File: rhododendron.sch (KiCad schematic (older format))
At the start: 43 parts, among them J1 Conn_02x20_Odd_Even, J2 Conn_02x20_Odd_Even, J3 Conn_02x08_Counter_Clockwise, J4 USB-A-SHIELDED, J5 USB-B-SHIELDED, J7 BONUS_ROW, U1 USB3343, Y1 26MHz

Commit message: r0.2: finalize for ordering; improve silkscreen; minor tweaks
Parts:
- added R8: DNP, Resistor_SMD:R_1206_3216Metric, symbol Device:R
- TP10, TP9: footprint TestPoint:TestPoint_Pad_D2.0mm -> gsg-modules:HEADER-1x1
- Y1: symbol Device:Crystal -> Device:Crystal_GND24
- renumbered C9 to C9-DNP1
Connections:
- net GND: now also Y1.2, Y1.4
- net PHY_XO: now also Y1.3; no longer Y1.2
- net TARGET_VBUS: now also R8.1, R8.2
- net PHY_26MHZ_IN renamed PHY_XI
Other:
- note added: "Microchip recommends <1R ESR\non VBUS capacitor. We're recommending DNP\nto limit inrush; the USB spec limits VBUS cap to 10uF."
- note added: "X"
- note removed: "Microchip recommends <1R ESR\non VBUS capacitor."
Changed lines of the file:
@@
 	4500 3650 5200 3650
 $Comp
-L Device:Crystal Y1
+L Device:Crystal_GND24 Y1
 U 1 1 5CD6A676
 P 6050 3450
@@
 Wire Wire Line
 	4500 2550 5450 2550
-Wire Wire Line
-	6400 2550 6750 2550
 $Comp
 L rhododendron:USB-A-SHIELDED J4
@@
 $EndComp
 Wire Wire Line
-	9100 3550 8300 3550
-Wire Wire Line
-	8300 3550 8300 2550
-Connection ~ 8300 2550
-Wire Wire Line
 	8400 2650 8400 3650
 Wire Wire Line
@@
 $EndComp
 $Comp
-L Device:C C9
-U 1 1 5CE810FA
-P 6750 2400
-F 0 "C9" H 6865 2446 50  0000 L CNN
-F 1 "2.2uF" H 6865 2355 50  0000 L CNN
-F 2 "gsg-modules:0603" H 6788 2250 50  0001 C CNN
-F 3 "~" H 6750 2400 50  0001 C CNN
-	1    6750 2400
-	1    0    0    -1
-$EndComp
-Connection ~ 6750 2550
-Wire Wire Line
-	6750 2550 8300 2550
-$Comp
 L power:GND #PWR0111
 U 1 1 5CE8181E
@@
 Wire Bus Line
 	2600 1500 2000 1500
-Wire Wire Line
-	5800 3600 5800 4100
-Wire Wire Line
-	5800 4100 6700 4100
-Connection ~ 5800 3600
-Wire Wire Line
-	5800 3600 6050 3600
 Text Notes 4500 4550 0    50   ~ 0
 Datasheet requries <1R ESR\nfor VDD33/VDD18 bypass.
@@
 Text Label 2000 1500 0    50   ~ 0
 ULPI_DATA
-Text Label 6700 4100 2    50   ~ 0
-PHY_26MHZ_IN
 Text Label 2750 2150 0    50   ~ 0
 ULPI_DATA0
@@
 USB_D+
 Text Notes 6300 2000 0    50   ~ 0
-Microchip recommends <1R ESR\non VBUS capacitor.
+Microchip recommends <1R ESR\non VBUS capacitor. We're recommending DNP\nto limit inrush; the USB spec limits VBUS cap to 10uF.
 $Comp
 L Device:LED D1
@@
 Connection ~ 5600 3600
 Wire Wire Line
-	5600 3600 5800 3600
-Wire Wire Line
 	5350 3600 5600 3600
 Wire Wire Line
@@
 Wire Wire Line
 	7600 5600 9600 5600
-Wire Wire Line
-	4500 2650 7500 2650
 Wire Wire Line
 	4500 2750 7600 2750
@@
 	1    0    0    -1
 $EndComp
-Connection ~ 8950 2550
-Wire Wire Line
-	8300 2550 8950 2550
 $Comp
 L Connector:TestPoint TP6
@@
 F 0 "TP10" H 11608 1022 50  0000 L CNN
 F 1 "TestPoint" H 11608 977 50  0001 L CNN
-F 2 "TestPoint:TestPoint_Pad_D2.0mm" H 11750 950 50  0001 C CNN
+F 2 "gsg-modules:HEADER-1x1" H 11750 950 50  0001 C CNN
 F 3 "~" H 11750 950 50  0001 C CNN
 	1    11550 950
@@
 F 0 "TP9" H 11258 1022 50  0000 L CNN
 F 1 "TestPoint" H 11258 977 50  0001 L CNN
-F 2 "TestPoint:TestPoint_Pad_D2.0mm" H 11400 950 50  0001 C CNN
+F 2 "gsg-modules:HEADER-1x1" H 11400 950 50  0001 C CNN
 F 3 "~" H 11400 950 50  0001 C CNN
 	1    11200 950
@@
 NoConn ~ 4450 -600
 NoConn ~ 10850 3300
-Connection ~ 8500 2750
 Connection ~ 8400 2650
 Wire Wire Line
@@
 Wire Wire Line
 	9600 3200 9050 3200
-Wire Wire Line
-	9100 2750 8500 2750
-Wire Wire Line
-	8950 2550 9100 2550
 $Comp
 L rhododendron:USB-B-SHIELDED J5
@@
 Wire Wire Line
 	7500 2950 7500 2650
-Connection ~ 7500 2650
 Wire Wire Line
 	7500 2650 8400 2650
-Connection ~ 7600 2750
-Wire Wire Line
-	7600 2750 8500 2750
 Wire Wire Line
 	7600 2750 7600 2950
 Wire Wire Line
 	4500 2850 4600 2850
-Wire Bus Line
-	2600 1500 2600 2750
-$Comp
-L power:GND #PWR?
+$Comp
+L power:GND #PWR0102
 U 1 1 5D44DC8D
 P 4600 2850
-F 0 "#PWR?" H 4600 2600 50  0001 C CNN
+F 0 "#PWR0102" H 4600 2600 50  0001 C CNN
 F 1 "GND" V 4605 2722 50  0000 R CNN
 F 2 "" H 4600 2850 50  0001 C CNN
@@
 	0    -1   -1   0
 $EndComp
+Wire Wire Line
+	5600 3600 6050 3600
+$Comp
+L Device:R R8
+U 1 1 5D2FC30C
+P 8650 3200
+F 0 "R8" H 8720 3246 50  0000 L CNN
+F 1 "DNP" H 8720 3155 50  0000 L CNN
+F 2 "Resistor_SMD:R_1206_3216Metric" V 8580 3200 50  0001 C CNN
+F 3 "~" H 8650 3200 50  0001 C CNN
+	1    8650 3200
+	1    0    0    -1
+$EndComp
+$Comp
+L Device:C C9-DNP1
+U 1 1 5CE810FA
+P 6750 2400
+F 0 "C9-DNP1" H 6865 2446 50  0000 L CNN
+F 1 "2.2uF" H 6865 2355 50  0000 L CNN
+F 2 "gsg-modules:0603" H 6788 2250 50  0001 C CNN
+F 3 "~" H 6750 2400 50  0001 C CNN
+	1    6750 2400
+	1    0    0    -1
+$EndComp
+$Comp
+L power:GND #PWR0114
+U 1 1 5D34565D
+P 5850 3450
+F 0 "#PWR0114" H 5850 3200 50  0001 C CNN
+F 1 "GND" V 6100 3450 50  0001 R CNN
+F 2 "" H 5850 3450 50  0001 C CNN
+F 3 "" H 5850 3450 50  0001 C CNN
+	1    5850 3450
+	0    1    1    0
+$EndComp
+$Comp
+L power:GND #PWR0118
+U 1 1 5D346051
+P 6450 3450
+F 0 "#PWR0118" H 6450 3200 50  0001 C CNN
+F 1 "GND" V 6700 3450 50  0001 R CNN
+F 2 "" H 6450 3450 50  0001 C CNN
+F 3 "" H 6450 3450 50  0001 C CNN
+	1    6450 3450
+	0    -1   -1   0
+$EndComp
+Wire Wire Line
+	6250 3450 6450 3450
+Connection ~ 7600 2750
+Wire Wire Line
+	7600 2750 8500 2750
+Connection ~ 8500 2750
+Connection ~ 7500 2650
+Wire Wire Line
+	4500 2650 7500 2650
+Wire Wire Line
+	6400 2550 6750 2550
+Connection ~ 6750 2550
+Wire Wire Line
+	6750 2550 8300 2550
+Connection ~ 8950 2550
+Wire Wire Line
+	8950 2550 9100 2550
+Wire Wire Line
+	8300 3550 8300 2550
+Connection ~ 8300 2550
+Wire Wire Line
+	8300 2550 8650 2550
+Wire Wire Line
+	8650 3050 8650 2550
+Connection ~ 8650 2550
+Wire Wire Line
+	8650 2550 8950 2550
+Wire Wire Line
+	8650 3350 8650 3550
+Wire Wire Line
+	8300 3550 8650 3550
+Connection ~ 8650 3550
+Wire Wire Line
+	8650 3550 9100 3550
+Wire Wire Line
+	9100 2750 8500 2750
+Wire Bus Line
+	2600 1500 2600 2750
+Text Notes 6600 2550 0    315  ~ 0
+X
+Text Notes 8500 3400 0    315  ~ 0
+X
 $EndSCHEMATC

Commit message: r0.3: capture schematic with all changes
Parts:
- removed C8: 8.2pF, gsg-modules:0603, symbol Device:C
- removed J3: Conn_02x08_Counter_Clockwise, gsg-modules:HEADER-2x8, symbol Connector_Generic:Conn_02x08_Counter_Clockwise
- removed Y1: 26MHz, gsg-modules:XTAL3.2x2.5mm, symbol Device:Crystal_GND24
- added D5: LED, LED_SMD:LED_0603_1608Metric_Pad1.05x0.95mm_HandSolder, symbol Device:LED
- added JP3: Jumper_NC_Small, symbol Device:Jumper_NC_Small
- added R10, R12, R9: 1K, symbol Device:R
- added R11, R15: 0R, symbol Device:R
- added R13: 1K5, symbol Device:R
- added R14: 10K, symbol Device:R
- added TP7: TestPoint, symbol Connector:TestPoint
- added U2: M24C02-FMN, Package_SO:SOIC-8_3.9x4.9mm_P1.27mm, symbol Memory_EEPROM:M24C02-FMN
- C7: value 8.2pF -> 10nF; footprint gsg-modules:0603 -> (none)
- J4: Manuf P/N 87583-2010BLF -> UE27AC54100
- JP1, JP2: footprint gsg-modules:0402-SHORT-10MIL -> (none)
- R2: value 1M -> 330
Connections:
- net ADC0_5 is gone; now on net PHY_VDD18: J7.4 (Pin_4)
- net P1_0 is gone; now on net ULPI_NXT: J1.7 (Pin_7)
- net P1_6 is gone; now on net ULPI_DIR: J1.16 (Pin_16)
- net P2_0 is gone; now on net ~PHY_RESET: J1.35 (Pin_35)
- net P2_3 is gone; now on net ULPI_DATA5: J2.20 (Pin_20)
- net P2_5 is gone; now on net REFCLK: J2.18 (Pin_18)
- net P7_2 is gone; now on net ULPI_DATA4: J2.23 (Pin_23)
- net VCC is gone; now on net +3V3: J7.20 (Pin_20)
- net +3V3: now also C7.2, R2.2, U1.2 (CLKOUT), R14.1, TP7.1, U2.8 (VCC)
- net GND: now also JP1.1, JP2.1, JP3.1, R13.2, U2.4 (VSS); no longer J7.10 (Pin_10)
- net I2C0_SCL: now also U2.6 (SCL)
- net I2C0_SDA: now also U2.5 (SDA)
- net LA_USB_D+: now also R10.2; no longer JP2.1
- net LA_USB_D-: now also R9.2; no longer JP1.1
- net TARGET_VBUS: now also R12.1
- net ULPI_DIR: now also R15.1, R15.2
- net ULPI_NXT: now also R11.1, R11.2
- net USB_D+: now also R10.1; no longer JP2.2
- net USB_D-: now also R9.1; no longer JP1.2
- net ~PHY_RESET: now also R14.2; no longer J1.36 (Pin_36)
- net CLK2 renamed REFCLK
- net REFCLK: now also TP4.1, U1.21 (REFCLK/XI)
- net LED_STATUS renamed LED_CAPTURING
- net P3_5 renamed TARGET_VBUS_DETECT
- net TARGET_VBUS_DETECT: now also R12.2, R13.1
- net P3_6 renamed I2C_EEPROM_WC
- net I2C_EEPROM_WC: now also U2.7 (~WC)
- net P5_2 renamed LED_ERROR
- net LED_ERROR: now also D5.1 (K)
- removed net PHY_XI: R2.2, U1.21 (REFCLK/XI)
- removed net PHY_XO: C7.2, R2.1, TP4.1, U1.20 (XO)
- removed net ULPI_CLK: J1.11 (Pin_11), J1.34 (Pin_34), U1.2 (CLKOUT)
- new net: D5.2 (A), R2.1
- new net: JP1.2, U2.1 (E0)
- new net: JP2.2, U2.2 (E1)
- new net: JP3.2, U2.3 (E2)
- new net CLK0: J1.11 (Pin_11)
- new net P6_3: J1.36 (Pin_36)
- new net P9_6: J1.34 (Pin_34)
- new net RTCX1: J7.10 (Pin_10)
- no-connect marks 76 -> 67
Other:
- note added: "1.8V to ADC for self-test"
- note added: "BLUE"
- note added: "DATA5/DATA4 carry the \npassive RXEvent bits for\nRXActive and RXError"
- note added: "DNP resistors on CLK/DIR for \npossible series termination;\nthese sensitive lines determine\npacket boundaries"
- note added: "GREEN"
- note added: "RED\n"
- note added: "note: CLKOUT connected to VDDIO\nselects a 60MHz CLKIN for the PHY"
- note added: "to SCT"
- note removed: "Debug Header (r0 only?)"
- note removed: "alternate method of clocking:\nuse GP_CLKIN to drive SGPIO,\nrather than using a slice shift clock"
- note removed: "author's note:\nthese may be a PITA to route,\nso they'll likely be dropped; nice debug though"
- note removed: "freq +/- 500ppm"
- moved on the sheet: D1, D2, D3, D4, J1, J2, J7, R4, R5, R6, R7

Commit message: r0.3: route the changes made in the r0.3 schematic
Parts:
- C7, R10, R11, R12, R13, R14, R15, R9: footprint (none) -> gsg-modules:0603
- JP1, JP2, JP3: footprint (none) -> gsg-modules:0402-SHORT-10MIL
- TP7: footprint (none) -> TestPoint:TestPoint_Pad_D2.0mm
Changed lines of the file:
@@
 EESchema Schematic File Version 4
 LIBS:rhododendron-cache
-EELAYER 29 0
+EELAYER 30 0
 EELAYER END
 $Descr USLedger 17000 11000
@@
 F 0 "R9" H 7350 3150 50  0000 L CNN
 F 1 "1K" H 7350 3050 50  0000 L CNN
-F 2 "" V 7430 3100 50  0001 C CNN
+F 2 "gsg-modules:0603" V 7430 3100 50  0001 C CNN
 F 3 "~" H 7500 3100 50  0001 C CNN
 	1    7500 3100
@@
 F 0 "R10" H 7650 3150 50  0000 L CNN
 F 1 "1K" H 7650 3050 50  0000 L CNN
-F 2 "" V 7530 3100 50  0001 C CNN
+F 2 "gsg-modules:0603" V 7530 3100 50  0001 C CNN
 F 3 "~" H 7600 3100 50  0001 C CNN
 	1    7600 3100
@@
 F 0 "R14" H 14100 6000 50  0000 L CNN
 F 1 "10K" H 14050 5900 50  0000 L CNN
-F 2 "" V 14180 5900 50  0001 C CNN
+F 2 "gsg-modules:0603" V 14180 5900 50  0001 C CNN
 F 3 "~" H 14250 5900 50  0001 C CNN
 	1    14250 5900
@@
 F 0 "R11" V 13350 5550 50  0000 C CNN
 F 1 "0R" V 13450 5550 50  0000 C CNN
-F 2 "" V 13380 5550 50  0001 C CNN
+F 2 "gsg-modules:0603" V 13380 5550 50  0001 C CNN
 F 3 "~" H 13450 5550 50  0001 C CNN
 	1    13450 5550
@@
 F 0 "R15" V 15800 6000 50  0000 C CNN
 F 1 "0R" V 15900 6000 50  0000 C CNN
-F 2 "" V 15830 6000 50  0001 C CNN
+F 2 "gsg-modules:0603" V 15830 6000 50  0001 C CNN
 F 3 "~" H 15900 6000 50  0001 C CNN
 	1    15900 6000
@@
 F 0 "R12" H 13570 3645 50  0000 L CNN
 F 1 "1K" H 13570 3555 50  0000 L CNN
-F 2 "" V 13430 3600 50  0001 C CNN
+F 2 "gsg-modules:0603" V 13430 3600 50  0001 C CNN
 F 3 "~" H 13500 3600 50  0001 C CNN
 	1    13500 3600
@@
 F 0 "R13" H 13570 4045 50  0000 L CNN
 F 1 "1K5" H 13570 3955 50  0000 L CNN
-F 2 "" V 13430 4000 50  0001 C CNN
+F 2 "gsg-modules:0603" V 13430 4000 50  0001 C CNN
 F 3 "~" H 13500 4000 50  0001 C CNN
 	1    13500 4000
@@
 F 0 "JP1" H 8600 8300 50  0000 C CNN
 F 1 "Jumper_NC_Small" H 8450 8370 50  0001 C CNN
-F 2 "" H 8450 8250 50  0001 C CNN
+F 2 "gsg-modules:0402-SHORT-10MIL" H 8450 8250 50  0001 C CNN
 F 3 "~" H 8450 8250 50  0001 C CNN
 	1    8450 8250
@@
 F 0 "JP2" H 8600 8400 50  0000 C CNN
 F 1 "Jumper_NC_Small" H 8450 8470 50  0001 C CNN
-F 2 "" H 8450 8350 50  0001 C CNN
+F 2 "gsg-modules:0402-SHORT-10MIL" H 8450 8350 50  0001 C CNN
 F 3 "~" H 8450 8350 50  0001 C CNN
 	1    8450 8350
@@
 F 0 "JP3" H 8600 8500 50  0000 C CNN
 F 1 "Jumper_NC_Small" H 8450 8570 50  0001 C CNN
-F 2 "" H 8450 8450 50  0001 C CNN
+F 2 "gsg-modules:0402-SHORT-10MIL" H 8450 8450 50  0001 C CNN
 F 3 "~" H 8450 8450 50  0001 C CNN
 	1    8450 8450
@@
 F 0 "TP7" H 8550 7850 50  0000 L CNN
 F 1 "TestPoint" H 8758 7878 50  0001 L CNN
-F 2 "" H 8900 7850 50  0001 C CNN
+F 2 "TestPoint:TestPoint_Pad_D2.0mm" H 8900 7850 50  0001 C CNN
 F 3 "~" H 8900 7850 50  0001 C CNN
 	1    8700 7850
@@
 F 0 "C7" V 9200 7750 50  0000 C CNN
 F 1 "10nF" V 9290 7750 50  0000 C CNN
-F 2 "" H 9488 7600 50  0001 C CNN
+F 2 "gsg-modules:0603" H 9488 7600 50  0001 C CNN
 F 3 "~" H 9450 7750 50  0001 C CNN
 	1    9450 7750

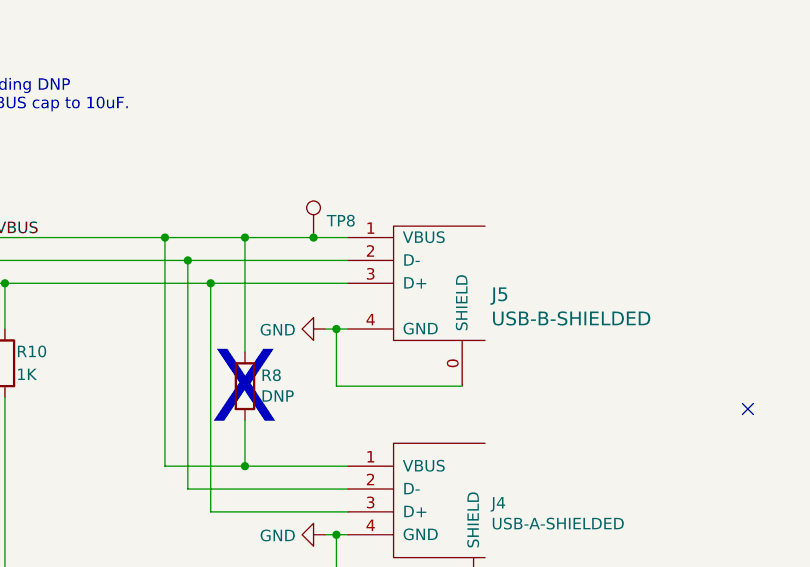
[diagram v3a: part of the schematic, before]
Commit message: r0.3: add 3d models and prepare for plotting
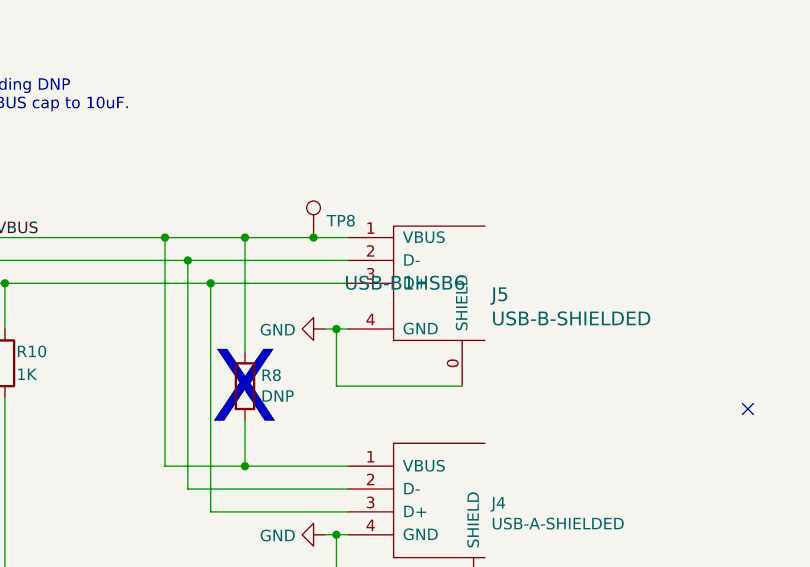
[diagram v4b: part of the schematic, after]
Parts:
- J5: footprint rhododendron:USB_B_OST_USB-B1HSxx_Horizontal -> rhododendron:USB_B_OST_USB-_Horizontal
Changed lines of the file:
@@
 F 0 "J5" H 9728 2700 60  0000 L CNN
 F 1 "USB-B-SHIELDED" H 9728 2594 60  0000 L CNN
-F 2 "rhododendron:USB_B_OST_USB-B1HSxx_Horizontal" H 9350 2750 60  0001 C CNN
-F 3 "" H 9350 2750 60  0000 C CNN
+F 2 "rhododendron:USB_B_OST_USB-_Horizontal" H 9350 2750 60  0001 C CNN
+F 3 "USB-B1HSB6" H 9350 2750 60  0000 C CNN
 	1    9350 2750
 	1    0    0    -1

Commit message: adopt OSHWA convention for SPI signal names https://www.oshwa.org/a-resolution-to-redefine-spi-signal-names
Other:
- note added: "CIPO"
- note added: "COPI"
- note added: "CS"
- note removed: "MISO"
- note removed: "MOSI"
- note removed: "SSEL"
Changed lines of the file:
@@
 I2C0_SCL
 Text Notes 14450 6150 2    40   ~ 0
-SSEL
+CS
 Text Notes 15450 6150 0    40   ~ 0
 SCK
 Text Notes 14450 6250 2    40   ~ 0
-MOSI
+COPI
 Text Notes 15450 6250 0    40   ~ 0
-MISO
+CIPO
 Text Label 14150 6050 2    40   ~ 0
 ~PHY_RESET
